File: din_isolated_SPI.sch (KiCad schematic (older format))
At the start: 4 parts, among them U1 SI8661AB-B-IS1, U2 MCP7940N, U3 BME280, U4 WeMos_mini

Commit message: Autorouted basic isolated SPI
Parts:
- removed U2: MCP7940N, Housings_SSOP:TSSOP-8_4.4x3mm_Pitch0.65mm, symbol MCP7940N
- removed U3: BME280, BME280, symbol BME280
- added C1, C2: 100nF, Capacitors_SMD:C_0402, symbol C_Small
- added J1: CONN_01X10, Connectors_Molex:Molex_MicroLatch-53253-1070_10x2.00mm_Straight, symbol CONN_01X10
- added R1, R10, R11, R12, R2, R3, R4, R5, R6, R7, R8, R9: 50R, Resistors_SMD:R_0402, symbol R_Small
- U1: footprint Housings_SOIC:SOIC-16_3.9x9.9mm_Pitch1.27mm -> Housings_SOIC:SOIC-16W_7.5x10.3mm_Pitch1.27mm
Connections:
- net labels added: +3V3, 3V3_C, 3V3_I, CLK_E, CLK_W, CS0_E, CS0_W, CS1_E, CS1_W, CS2_E, CS2_W, GNDD, GNDS, GND_C, GND_I, MISO_E, MISO_W, MOSI_E, MOSI_W
- wire segments 0 -> 58
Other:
- moved on the sheet: U1, U4

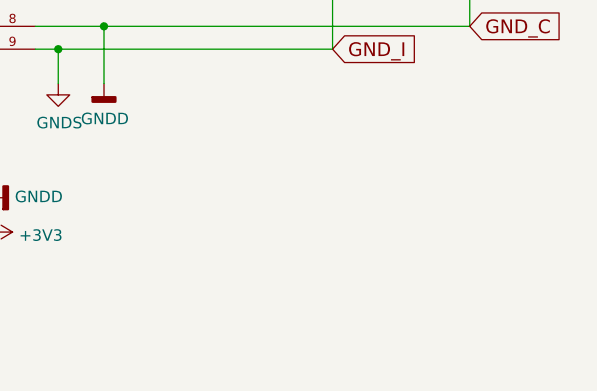
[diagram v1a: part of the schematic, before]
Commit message: Added logos
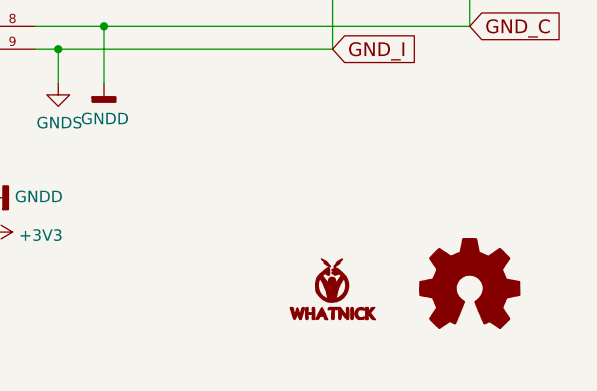
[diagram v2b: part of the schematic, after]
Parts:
- added G1: LOGO, Whatnick_logo:Whatnick_logo, symbol LOGO
- added LOGO1: Logo_Open_Hardware_Small, Symbols:OSHW-Symbol_6.7x6mm_SilkScreen, symbol Logo_Open_Hardware_Small
- U1: footprint Housings_SOIC:SOIC-16W_7.5x10.3mm_Pitch1.27mm -> Housings_SOIC:SOIC-16_3.9x9.9mm_Pitch1.27mm
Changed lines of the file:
@@
 LIBS:wemos_mini
 LIBS:BME280
+LIBS:whatnick
+LIBS:graphic_symbols
 LIBS:din_isolated_SPI-cache
 EELAYER 26 0
@@
 F 0 "U1" H 4700 4070 50  0000 C CNN
 F 1 "SI8661AB-B-IS1" H 4700 3979 50  0000 C CNN
-F 2 "Housings_SOIC:SOIC-16W_7.5x10.3mm_Pitch1.27mm" H 4700 3200 50  0001 L BNN
+F 2 "Housings_SOIC:SOIC-16_3.9x9.9mm_Pitch1.27mm" H 4700 3200 50  0001 L BNN
 F 3 "Silicon Labs" H 4700 3200 50  0001 L BNN
 F 4 "2.12 USD" H 4700 3200 50  0001 L BNN "Price"
@@
 Text GLabel 4200 4450 1    60   Input ~ 0
 GND_I
+$Comp
+L LOGO G1
+U 1 1 59F5EAB7
+P 6900 4850
+F 0 "G1" H 6900 4748 60  0001 C CNN
+F 1 "LOGO" H 6900 4952 60  0001 C CNN
+F 2 "Whatnick_logo:Whatnick_logo" H 6900 4850 60  0001 C CNN
+F 3 "" H 6900 4850 60  0001 C CNN
+	1    6900 4850
+	1    0    0    -1
+$EndComp
+$Comp
+L Logo_Open_Hardware_Small LOGO1
+U 1 1 59F5EC0C
+P 7500 4850
+F 0 "LOGO1" H 7500 5125 50  0001 C CNN
+F 1 "Logo_Open_Hardware_Small" H 7500 4625 50  0001 C CNN
+F 2 "Symbols:OSHW-Symbol_6.7x6mm_SilkScreen" H 7500 4850 50  0001 C CNN
+F 3 "" H 7500 4850 50  0001 C CNN
+	1    7500 4850
+	1    0    0    -1
+$EndComp
 $EndSCHEMATC

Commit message: Change to 0603 and reroute
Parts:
- C1, C2: footprint Capacitors_SMD:C_0402 -> Capacitors_SMD:C_0603
- R1, R10, R11, R12, R2, R3, R4, R5, R6, R7, R8, R9: footprint Resistors_SMD:R_0402 -> Resistors_SMD:R_0603
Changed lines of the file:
@@
 F 0 "C1" H 6992 3396 50  0000 L CNN
 F 1 "100nF" H 6992 3305 50  0000 L CNN
-F 2 "Capacitors_SMD:C_0402" H 6900 3350 50  0001 C CNN
+F 2 "Capacitors_SMD:C_0603" H 6900 3350 50  0001 C CNN
 F 3 "" H 6900 3350 50  0001 C CNN
 	1    6900 3350
@@
 F 0 "C2" H 7592 3396 50  0000 L CNN
 F 1 "100nF" H 7592 3305 50  0000 L CNN
-F 2 "Capacitors_SMD:C_0402" H 7500 3350 50  0001 C CNN
+F 2 "Capacitors_SMD:C_0603" H 7500 3350 50  0001 C CNN
 F 3 "" H 7500 3350 50  0001 C CNN
 	1    7500 3350
@@
 F 0 "R1" V 3400 3200 50  0000 C CNN
 F 1 "50R" V 3400 3050 50  0000 C CNN
-F 2 "Resistors_SMD:R_0402" H 3450 2900 50  0001 C CNN
+F 2 "Resistors_SMD:R_0603" H 3450 2900 50  0001 C CNN
 F 3 "" H 3450 2900 50  0001 C CNN
 	1    3450 2900
@@
 F 0 "R2" V 3400 3300 50  0000 C CNN
 F 1 "50R" V 3400 3150 50  0000 C CNN
-F 2 "Resistors_SMD:R_0402" H 3450 3000 50  0001 C CNN
+F 2 "Resistors_SMD:R_0603" H 3450 3000 50  0001 C CNN
 F 3 "" H 3450 3000 50  0001 C CNN
 	1    3450 3000
@@
 F 0 "R3" V 3400 3400 50  0000 C CNN
 F 1 "50R" V 3400 3250 50  0000 C CNN
-F 2 "Resistors_SMD:R_0402" H 3450 3100 50  0001 C CNN
+F 2 "Resistors_SMD:R_0603" H 3450 3100 50  0001 C CNN
 F 3 "" H 3450 3100 50  0001 C CNN
 	1    3450 3100
@@
 F 0 "R4" V 3400 3600 50  0000 C CNN
 F 1 "50R" V 3400 3450 50  0000 C CNN
-F 2 "Resistors_SMD:R_0402" H 3450 3300 50  0001 C CNN
+F 2 "Resistors_SMD:R_0603" H 3450 3300 50  0001 C CNN
 F 3 "" H 3450 3300 50  0001 C CNN
 	1    3450 3300
@@
 F 0 "R5" V 3400 3700 50  0000 C CNN
 F 1 "50R" V 3400 3550 50  0000 C CNN
-F 2 "Resistors_SMD:R_0402" H 3450 3400 50  0001 C CNN
+F 2 "Resistors_SMD:R_0603" H 3450 3400 50  0001 C CNN
 F 3 "" H 3450 3400 50  0001 C CNN
 	1    3450 3400
@@
 F 0 "R6" V 3400 3800 50  0000 C CNN
 F 1 "50R" V 3400 3650 50  0000 C CNN
-F 2 "Resistors_SMD:R_0402" H 3450 3500 50  0001 C CNN
+F 2 "Resistors_SMD:R_0603" H 3450 3500 50  0001 C CNN
 F 3 "" H 3450 3500 50  0001 C CNN
 	1    3450 3500
@@
 F 0 "R7" V 5900 3200 50  0000 C CNN
 F 1 "50R" V 5900 3050 50  0000 C CNN
-F 2 "Resistors_SMD:R_0402" H 5950 2900 50  0001 C CNN
+F 2 "Resistors_SMD:R_0603" H 5950 2900 50  0001 C CNN
 F 3 "" H 5950 2900 50  0001 C CNN
 	1    5950 2900
@@
 F 0 "R8" V 5900 3300 50  0000 C CNN
 F 1 "50R" V 5900 3150 50  0000 C CNN
-F 2 "Resistors_SMD:R_0402" H 5950 3000 50  0001 C CNN
+F 2 "Resistors_SMD:R_0603" H 5950 3000 50  0001 C CNN
 F 3 "" H 5950 3000 50  0001 C CNN
 	1    5950 3000
@@
 F 0 "R9" V 5900 3400 50  0000 C CNN
 F 1 "50R" V 5900 3250 50  0000 C CNN
-F 2 "Resistors_SMD:R_0402" H 5950 3100 50  0001 C CNN
+F 2 "Resistors_SMD:R_0603" H 5950 3100 50  0001 C CNN
 F 3 "" H 5950 3100 50  0001 C CNN
 	1    5950 3100
@@
 F 0 "R10" V 5900 3600 50  0000 C CNN
 F 1 "50R" V 5900 3450 50  0000 C CNN
-F 2 "Resistors_SMD:R_0402" H 5950 3300 50  0001 C CNN
+F 2 "Resistors_SMD:R_0603" H 5950 3300 50  0001 C CNN
 F 3 "" H 5950 3300 50  0001 C CNN
 	1    5950 3300
@@
 F 0 "R11" V 5900 3700 50  0000 C CNN
 F 1 "50R" V 5900 3550 50  0000 C CNN
-F 2 "Resistors_SMD:R_0402" H 5950 3400 50  0001 C CNN
+F 2 "Resistors_SMD:R_0603" H 5950 3400 50  0001 C CNN
 F 3 "" H 5950 3400 50  0001 C CNN
 	1    5950 3400
@@
 F 0 "R12" V 5900 3800 50  0000 C CNN
 F 1 "50R" V 5900 3650 50  0000 C CNN
-F 2 "Resistors_SMD:R_0402" H 5950 3500 50  0001 C CNN
+F 2 "Resistors_SMD:R_0603" H 5950 3500 50  0001 C CNN
 F 3 "" H 5950 3500 50  0001 C CNN
 	1    5950 3500
